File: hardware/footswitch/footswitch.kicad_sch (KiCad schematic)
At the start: 2 parts, among them J1 Conn_02x05_Counter_Clockwise

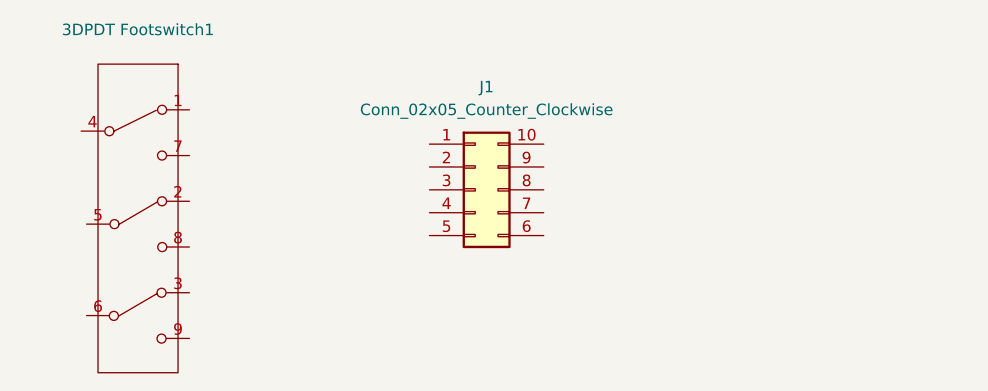
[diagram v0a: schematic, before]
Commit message: Connect up footswitch to IDC 2 x 5
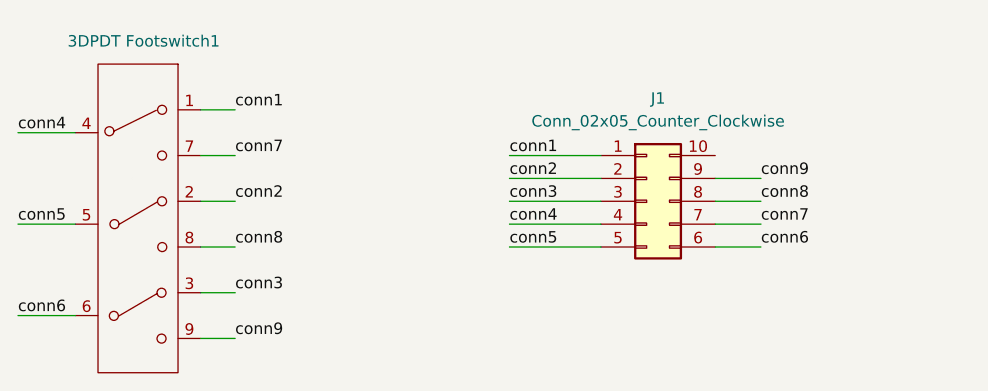
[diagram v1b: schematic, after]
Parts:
- 3DPDT Footswitch1: footprint (none) -> Button_Switch_THT:Switches_Stomp_Switch_3PDT
- J1: footprint (none) -> Connector_IDC:IDC-Header_2x05_P2.54mm_Latch6.5mm_Vertical
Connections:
- net conn1: now reaches 3DPDT Footswitch1.1 (A)
- net conn1: now also J1.1 (Pin_1)
- net conn2: now reaches 3DPDT Footswitch1.2 (B)
- net conn2: now also J1.2 (Pin_2)
- net conn3: now reaches 3DPDT Footswitch1.3 (C)
- net conn3: now also J1.3 (Pin_3)
- net conn4: now reaches 3DPDT Footswitch1.4 (D)
- net conn4: now also J1.4 (Pin_4)
- net conn5: now reaches 3DPDT Footswitch1.5 (E)
- net conn5: now also J1.5 (Pin_5)
- net conn6: now reaches 3DPDT Footswitch1.6 (F)
- net conn6: now also J1.6 (Pin_6)
- net conn7: now reaches 3DPDT Footswitch1.7 (G)
- net conn7: now also J1.7 (Pin_7)
- net conn8: now reaches 3DPDT Footswitch1.8 (G)
- net conn8: now also J1.8 (Pin_8)
- net conn9: now reaches 3DPDT Footswitch1.9 (G)
- net conn9: now also J1.9 (Pin_9)
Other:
- moved on the sheet: J1

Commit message: Wider traces for footswitch PCB and connect main board
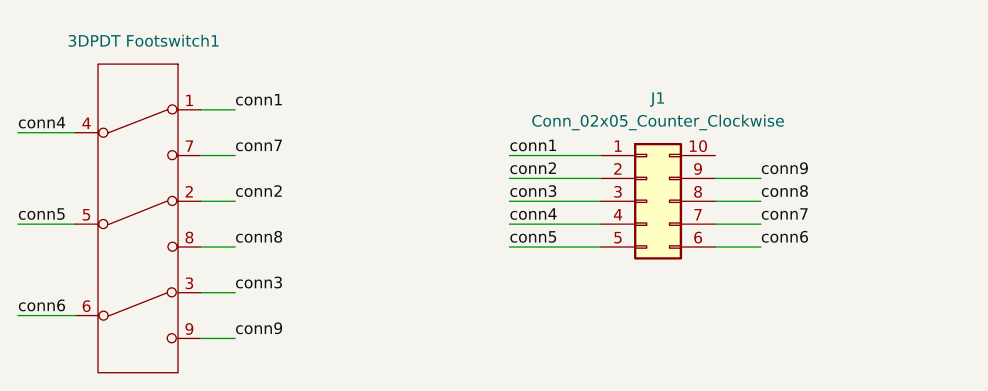
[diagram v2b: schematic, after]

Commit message: Add bypass LED and resistor to footswitch board
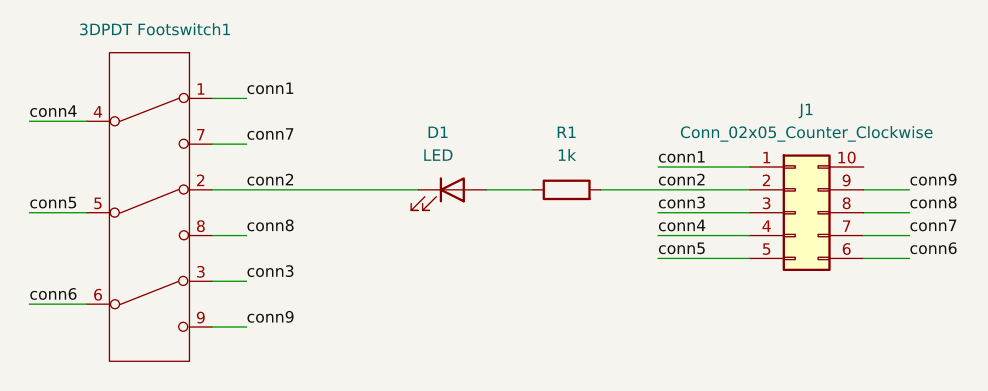
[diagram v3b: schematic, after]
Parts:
- added D1: LED, symbol Device:LED
- added R1: 1k, symbol Device:R
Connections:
- net conn2: now also D1.1 (K), R1.2
- new net: D1.2 (A), R1.1
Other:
- moved on the sheet: 3DPDT Footswitch1, J1

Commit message: Resize footswitch board, adjust footprints
Resistor and diode added
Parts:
- D1: footprint (none) -> LED_THT:LED_D1.8mm_W3.3mm_H2.4mm
- J1: footprint Connector_IDC:IDC-Header_2x05_P2.54mm_Latch6.5mm_Vertical -> Connector_IDC:IDC-Header_2x05_P2.54mm_Vertical
- R1: footprint (none) -> Resistor_THT:R_Axial_DIN0207_L6.3mm_D2.5mm_P10.16mm_Horizontal
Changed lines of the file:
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@@
 	(title_block
 		(title "3DPDT Footswitch board")
-		(date "2025-07-14")
+		(date "2025-08-14")
 		(rev "0.1")
 		(comment 1 "Denis Crowdy")
@@
 			)
 		)
-		(property "Footprint" ""
+		(property "Footprint" "Resistor_THT:R_Axial_DIN0207_L6.3mm_D2.5mm_P10.16mm_Horizontal"
 			(at 173.99 97.028 90)
 			(effects
@@
 			)
 		)
-		(property "Footprint" "Connector_IDC:IDC-Header_2x05_P2.54mm_Latch6.5mm_Vertical"
+		(property "Footprint" "Connector_IDC:IDC-Header_2x05_P2.54mm_Vertical"
 			(at 199.39 97.79 0)
 			(effects
@@
 			)
 		)
-		(property "Footprint" ""
+		(property "Footprint" "LED_THT:LED_D1.8mm_W3.3mm_H2.4mm"
 			(at 161.29 95.25 0)
 			(effects

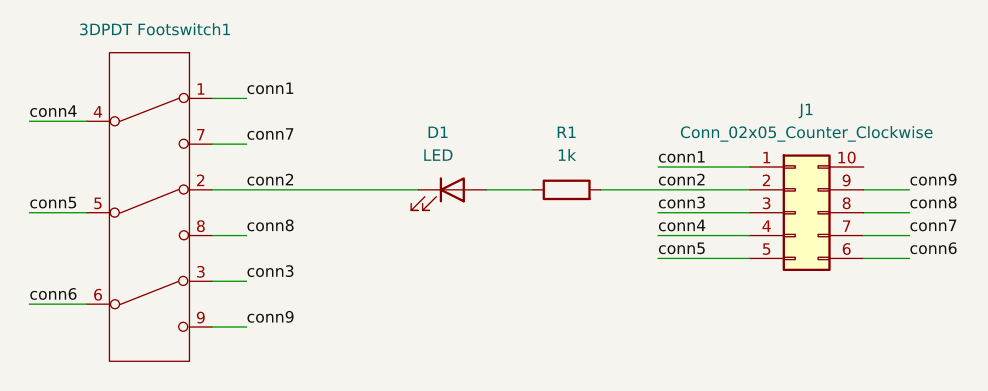
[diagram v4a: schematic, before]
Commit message: Connect everything with traces
Corrected schematic with fsw2
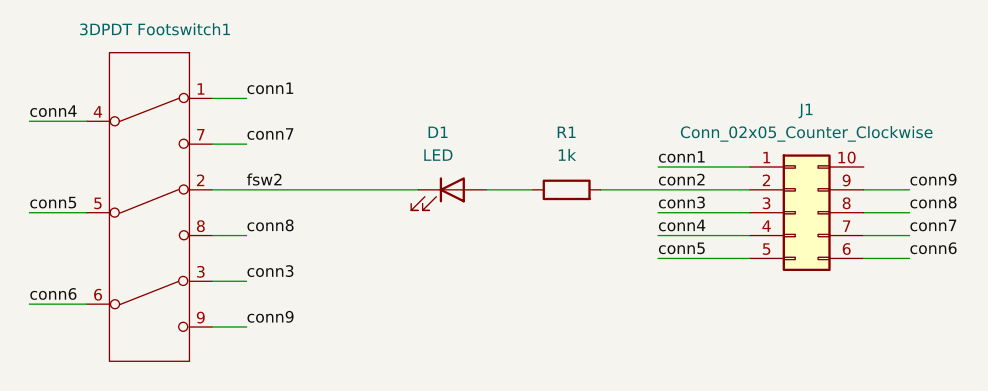
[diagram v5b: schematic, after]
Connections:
- net conn2: no longer 3DPDT Footswitch1.2 (B), D1.1 (K)
- new net fsw2: 3DPDT Footswitch1.2 (B), D1.1 (K)
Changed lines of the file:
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@@
 		)
 	)
-	(label "conn2"
+	(label "fsw2"
 		(at 138.43 95.25 0)
 		(effects
